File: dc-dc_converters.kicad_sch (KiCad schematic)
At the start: 63 parts, among them J3 JST_SH_1x4_SM04B-SRSS-TB-LF-SN, J4 Molex_Nano-Fit_1x2_105313-220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, U2 SIC477ED-T1-GE3, U3 AP62301Z6-7, U4 AP62301Z6-7

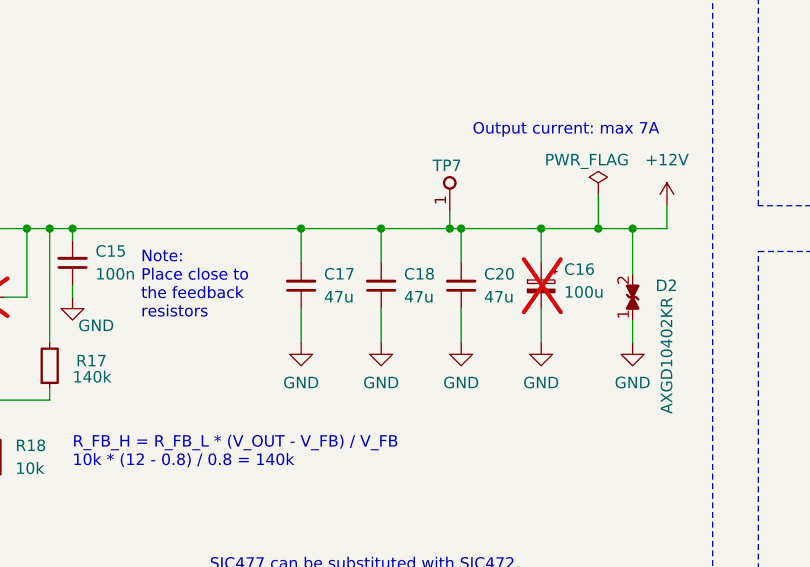
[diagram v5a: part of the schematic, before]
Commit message: [#57225] Change C17, C18, C20
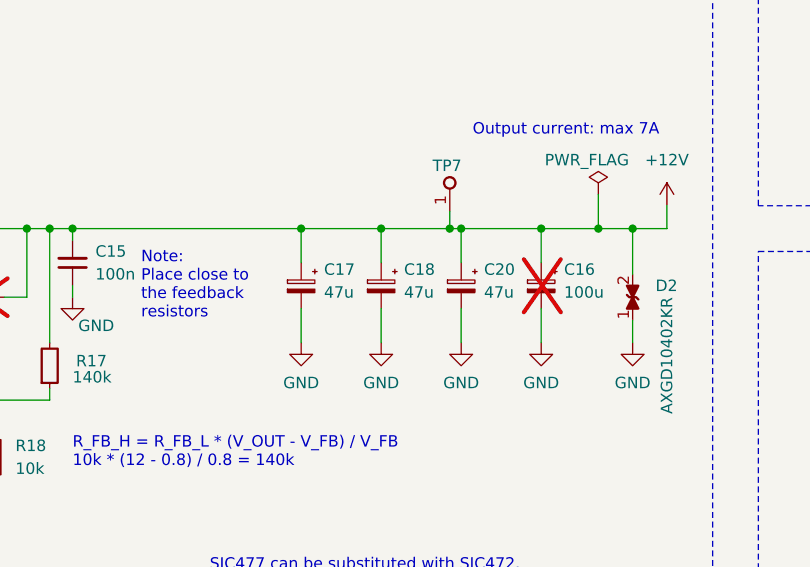
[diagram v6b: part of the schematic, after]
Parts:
- removed C17, C18, C20: C_47u_25V_1206, antmicro-footprints:C_1206_3216Metric, symbol antmicroCapacitorsmisc:C_47u_25V_1206
- added C17, C18, C20: C_Pol_47u_16V_EIA-B, antmicro-footprints:C_Pol_EIA-B, symbol antmicroCapacitorspol:C_Pol_47u_16V_EIA-B
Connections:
- net +12V: now also C17.1, C18.1, C20.1
- net GND: now also C17.2, C18.2, C20.2

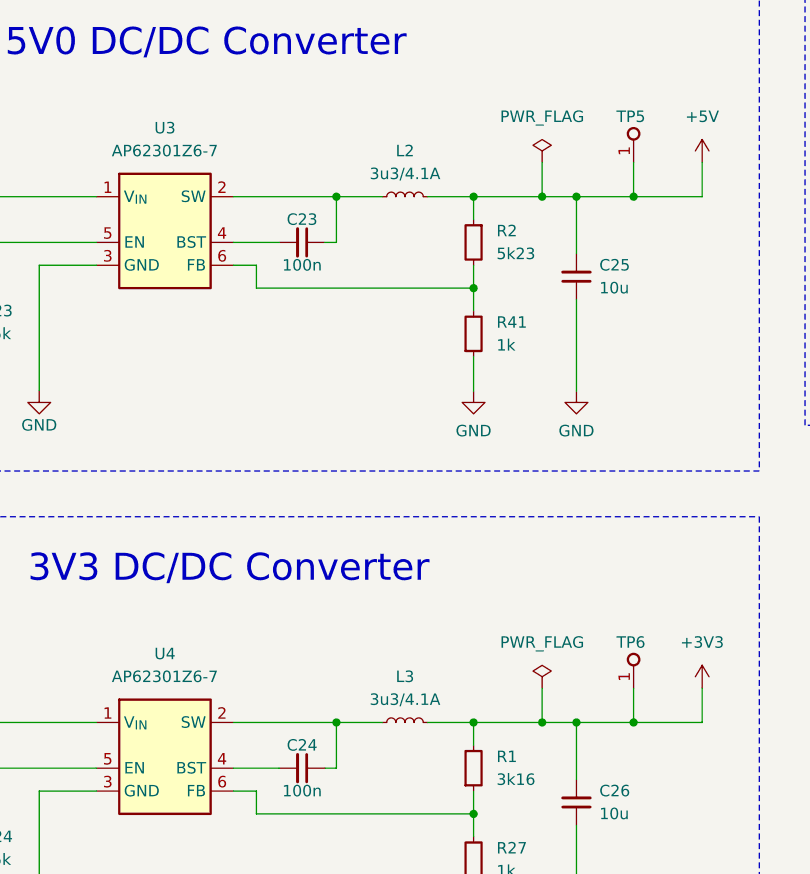
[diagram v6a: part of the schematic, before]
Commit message: [#57225] Change L2, L3
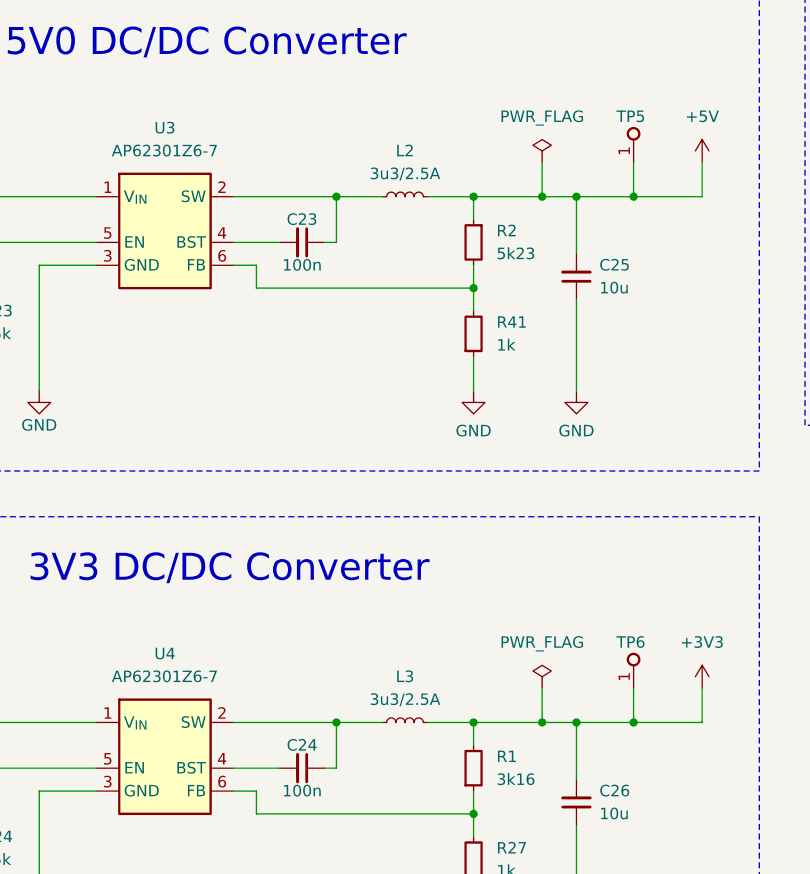
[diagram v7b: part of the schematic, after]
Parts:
- removed L2, L3: L_3u3_4.1A_WE-LHMI-5030, antmicro-footprints:L_WE-LHMI-5030, symbol antmicroFixedInductors:L_3u3_4.1A_WE-LHMI-5030
- added L2, L3: L_3u3_2.5A_1008, antmicro-footprints:L_1008_2520Metric, symbol antmicroFixedInductors:L_3u3_2.5A_1008
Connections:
- net +3V3: now also L3.2
- net +5V: now also L2.2
- net at C23.1, U3.2 (SW): now also L2.1
- net at C24.1, U4.2 (SW): now also L3.1

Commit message: [#57607] Update symbols from library
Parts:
- D5: Manufacturer (none) -> Littelfuse
- R17: Manufacturer template_manufacturer -> Vishay
- R18: Manufacturer template_manufacturer -> Bourns
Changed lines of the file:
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@@
       (effects (font (size 1.27 1.27) (thickness 0.15)) (justify left bottom) hide)
     )
-    (property "Datasheet" "https://www.mouser.pl/datasheet/2/240/media-3320461.pdf" (at 318.77 35.56 0)
+    (property "Datasheet" "https://www.mouser.com/datasheet/2/240/media-3320461.pdf" (at 318.77 35.56 0)
       (effects (font (size 1.27 1.27) (thickness 0.15)) (justify left bottom) hide)
     )
@@
       (effects (font (size 1.27 1.27) (thickness 0.15)) (justify left bottom) hide)
     )
+    (property "Manufacturer" "Littelfuse" (at 328.93 46.99 0)
+      (effects (font (size 1.27 1.27) (thickness 0.15)) (justify left bottom) hide)
+    )
     (pin "1")
     (pin "2")
@@
       (effects (font (size 1.27 1.27)) (justify right))
     )
-    (property "Manufacturer" "template_manufacturer" (at 218.44 71.12 0)
+    (property "Manufacturer" "Vishay" (at 218.44 71.12 0)
       (effects (font (size 1.27 1.27) (thickness 0.15)) (justify left bottom) hide)
     )
@@
       (effects (font (size 1.27 1.27) (thickness 0.15)) (justify left bottom) hide)
     )
-    (property "Datasheet" "https://www.mouser.pl/datasheet/2/447/YAGEO_PYu_RC_Group_51_RoHS_L_12-3313492.pdf" (at 146.05 215.9 0)
+    (property "Datasheet" "https://www.mouser.com/datasheet/2/447/YAGEO_PYu_RC_Group_51_RoHS_L_12-3313492.pdf" (at 146.05 215.9 0)
       (effects (font (size 1.27 1.27) (thickness 0.15)) (justify left bottom) hide)
     )
@@
       (effects (font (size 1.27 1.27) (thickness 0.15)) (justify left bottom) hide)
     )
-    (property "Datasheet" "https://www.mouser.pl/datasheet/2/54/CRT-1649066.pdf" (at 207.01 81.28 0)
+    (property "Datasheet" "https://www.mouser.com/datasheet/2/54/CRT-1649066.pdf" (at 207.01 81.28 0)
       (effects (font (size 1.27 1.27) (thickness 0.15)) (justify left bottom) hide)
     )
@@
       (effects (font (size 1.27 1.27)) (justify right))
     )
-    (property "Manufacturer" "template_manufacturer" (at 212.09 81.28 0)
+    (property "Manufacturer" "Bourns" (at 212.09 81.28 0)
       (effects (font (size 1.27 1.27) (thickness 0.15)) (justify left bottom) hide)
     )
